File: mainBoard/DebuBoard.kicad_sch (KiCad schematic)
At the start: 24 parts, among them J23 Conn_01x05, J24 Conn_01x04, J25 Conn_01x05, J26 Conn_01x05, J27 Conn_01x05, J28 Conn_01x04, J29 Conn_01x04, J30 Conn_01x04, J31 Conn_02x05_Odd_Even, J32 Conn_02x07_Odd_Even, J33 Conn_01x04, J34 Conn_01x02, J35 Conn_01x02, J36 Conn_01x03, J37 Conn_01x02, J38 Conn_01x02

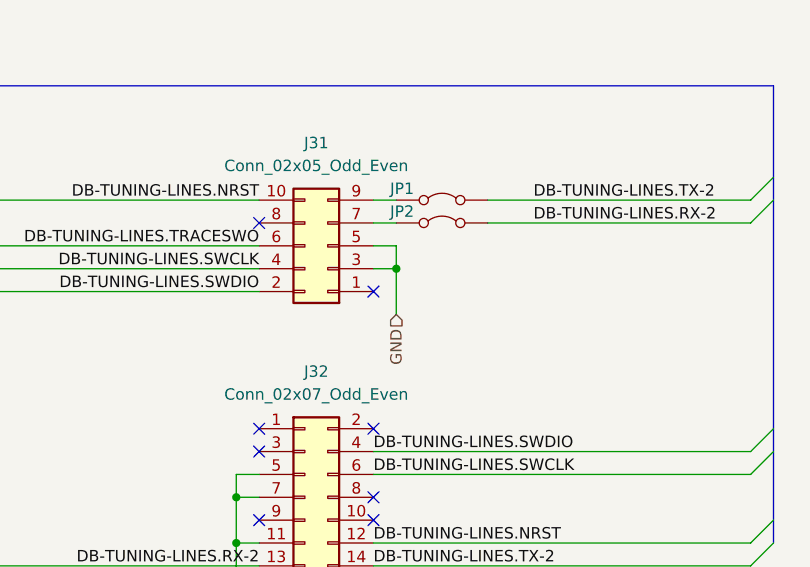
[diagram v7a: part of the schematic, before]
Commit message: On debug board: vire VRef (3v3) to the BMDU connector
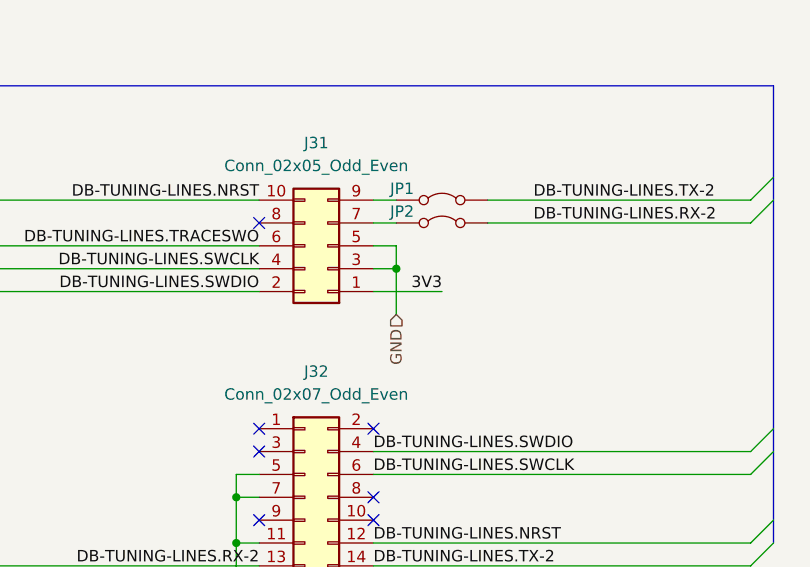
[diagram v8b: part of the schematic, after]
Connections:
- net 3V3: now also J31.1 (Pin_1)
- no-connect marks 8 -> 7
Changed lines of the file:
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@@
-	)
-	(no_connect
-		(at 133.35 60.96)
 	)
 	(no_connect
@@
 		(pts
 			(xy 133.35 53.34) (xy 135.89 53.34)
+		)
+		(stroke
+			(width 0)
+			(type default)
+		)
+	)
+	(wire
+		(pts
+			(xy 140.97 60.96) (xy 133.35 60.96)
 		)
 		(stroke
@@
 		(fields_autoplaced yes)
 		(effects
+			(font
+				(size 1.27 1.27)
+			)
+			(justify right bottom)
+		)
+	)
+	(label "3V3"
+		(at 140.97 60.96 180)
+		(fields_autoplaced yes)
+		(effects
